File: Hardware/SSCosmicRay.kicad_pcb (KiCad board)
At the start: 2 copper layers, 80 x 50 mm, 142 parts, among them J1 ICSP-CORTEX, J2 CONN-9, U1 AD8616, U10 TPS73130, U2 AD8616, U3 AD8616, U4 STM32L151C6T6, U5 LM2903DT, U6 AD8616, U7 AD8616, U8 AOZ1280, U9 MAX5026, X1 8MHz

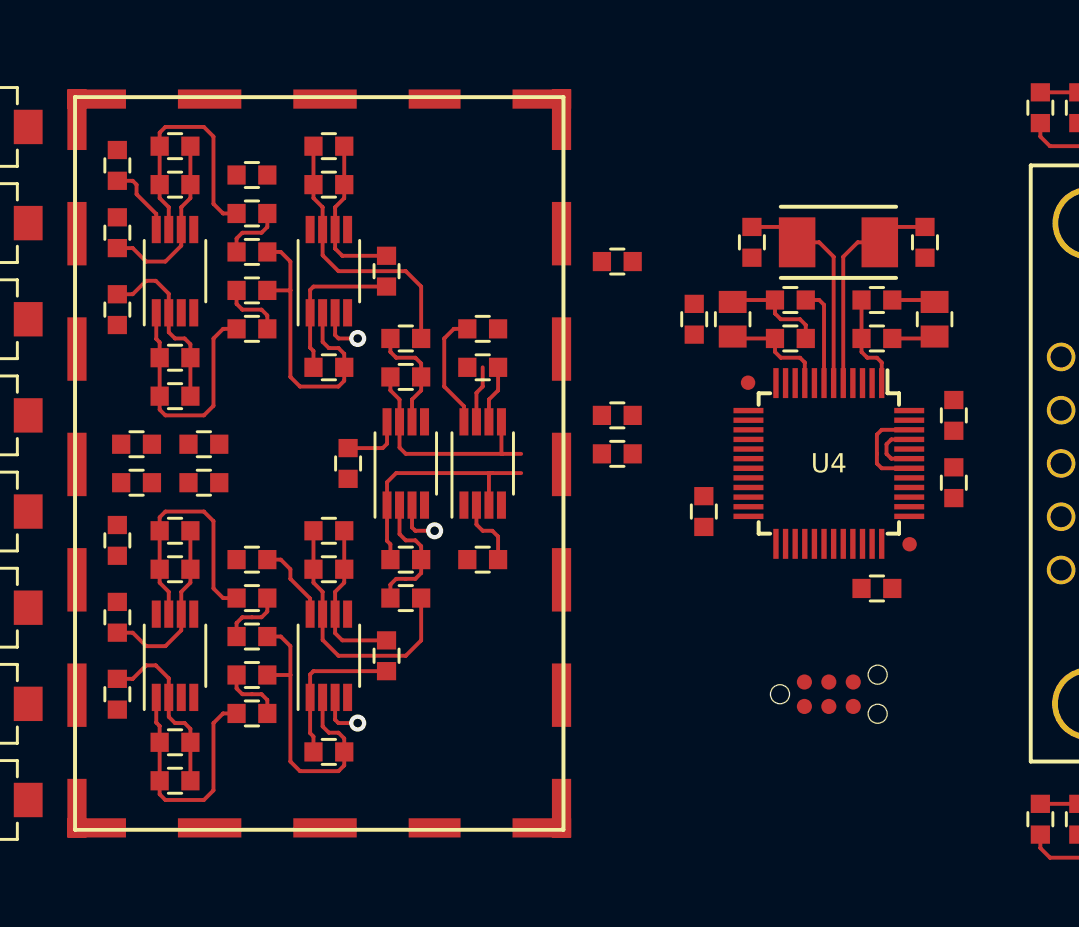
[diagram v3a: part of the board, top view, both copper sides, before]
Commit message: Equalize feedback network spacing
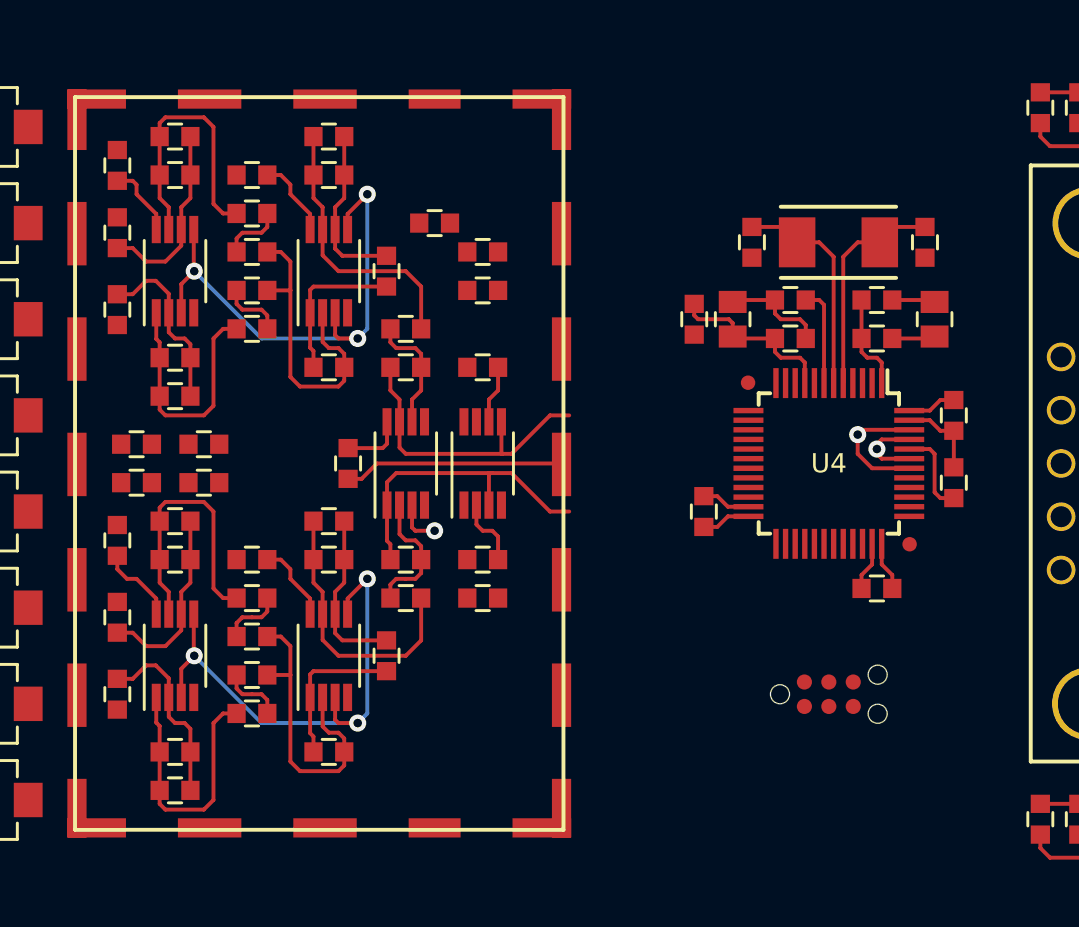
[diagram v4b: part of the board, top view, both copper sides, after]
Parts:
- moved R19 11.0 mm to (166.0, 67.0)
- moved R18 10.3 mm to (166.0, 85.0)
- moved R15 7.16 mm to (166.0, 69.0)
- moved C26 6.04 mm to (163.5, 65.5)
- moved C29 0.50 mm to (158.0, 83.0)
- moved C3 0.50 mm to (158.0, 63.0)
- moved C33 0.50 mm to (150.0, 93.0)
- moved C34 0.50 mm to (150.0, 83.0)
- moved C8 0.50 mm to (150.0, 63.0)
- moved R10 0.50 mm to (150.0, 61.0)
- moved R29 0.50 mm to (158.0, 81.0)
- moved R32 0.50 mm to (150.0, 95.0)
- moved R33 0.50 mm to (150.0, 81.0)
- moved R6 0.50 mm to (158.0, 61.0)
- moved R7 0.50 mm to (162.0, 71.0)
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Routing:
- net /Detector 1/Ref: track 7.22 -> 56.3 mm, vias 3 -> 7
- net GND: track 7.73 -> 28.7 mm
- net VAA: track 11.3 -> 19.6 mm
- net /Processor/BOOT: track 0.00 -> 4.55 mm
- net /Processor/A1: track 12.0 -> 15.8 mm
- net +3.3VADC: track 5.79 -> 9.25 mm
- net /Processor/A2: track 13.1 -> 16.4 mm
- net /Processor/DET1: track 2.97 -> 0.00 mm
- net /Processor/DO: track 5.07 -> 6.77 mm, vias 0 -> 1
- net +3.3V: track 12.4 -> 13.9 mm
- net N-000009: track 13.3 -> 14.3 mm
- net N-0000089: track 13.1 -> 14.1 mm
- net N-0000081: track 13.3 -> 14.3 mm
- net /Processor/DI: track 3.07 -> 4.07 mm, vias 0 -> 1
- net N-0000091: track 9.33 -> 9.83 mm
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
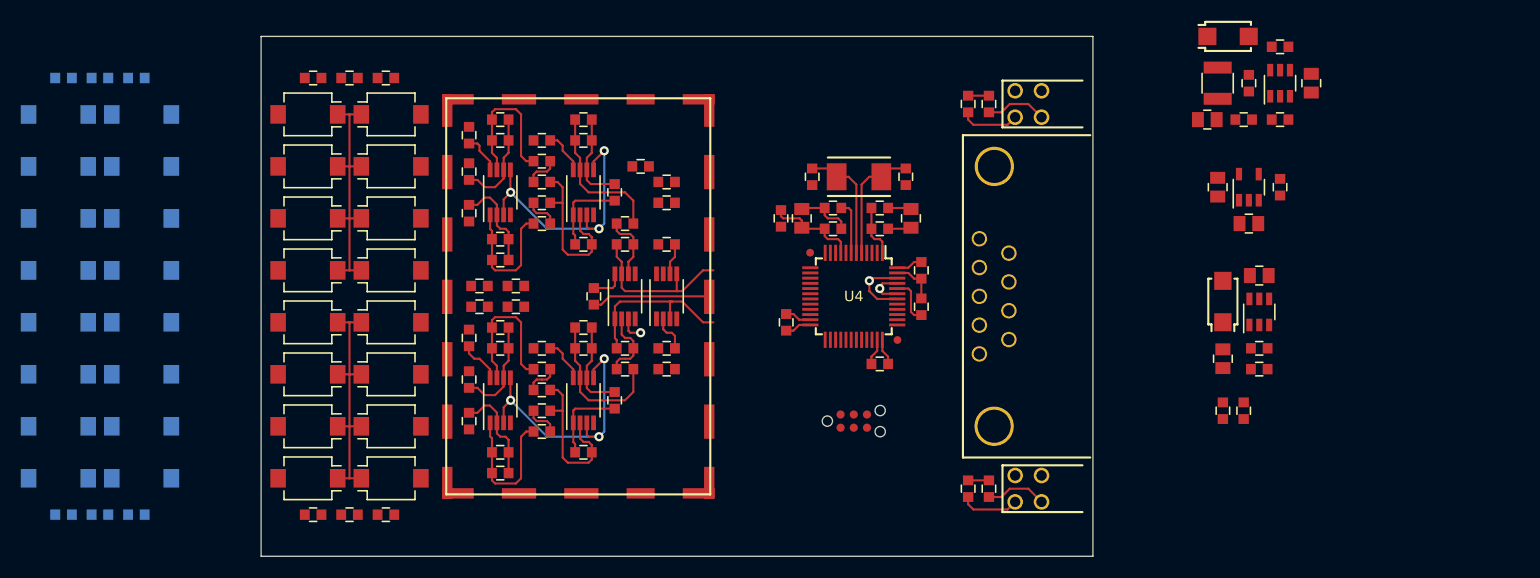
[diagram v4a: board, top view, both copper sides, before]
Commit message: Move interface connector to root sheet
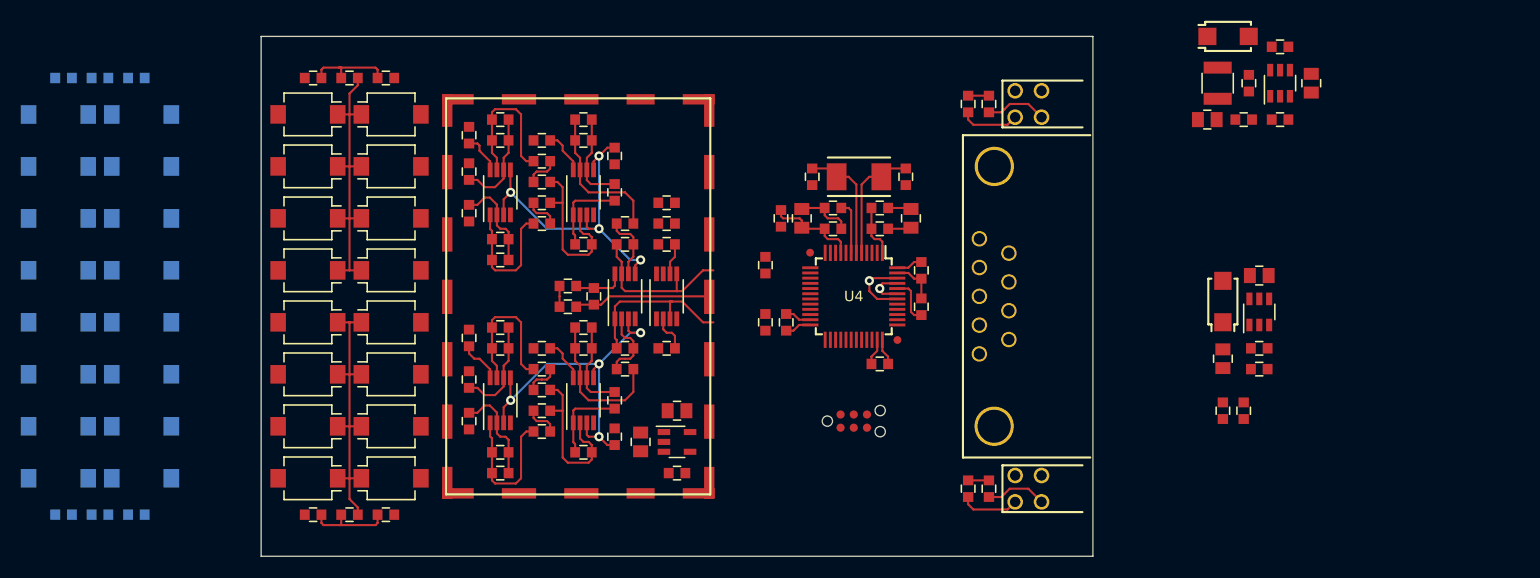
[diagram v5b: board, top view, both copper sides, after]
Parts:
- moved C45 64.2 mm to (167.0, 95.0), turned to 180 degrees
- moved C44 62.2 mm to (163.5, 92.0), turned to 270 degrees
- moved U10 60.2 mm to (167.0, 92.0), turned to 270 degrees
- moved C46 56.3 mm to (167.0, 89.0), turned to 180 degrees
- moved C47 19.5 mm to (161.0, 91.5), turned to 90 degrees
- moved R43 19.5 mm to (161.0, 64.5), turned to 90 degrees
- moved R19 12.4 mm to (175.5, 75.0), turned to 270 degrees
- moved R18 10.5 mm to (175.5, 80.5), turned to 90 degrees
- moved C30 5.00 mm to (156.5, 79.0)
- moved R42 5.00 mm to (156.5, 77.0)
- moved C26 4.30 mm to (166.0, 69.0)
- moved R15 2.00 mm to (166.0, 71.0)
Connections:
- net /Processor/AOUT renamed /Processor/AOut
- U4 pad 16: (no net) -> /Processor/DET1
- U4 pad 17: (no net) -> /Processor/A1
- U4 pad 19: (no net) -> /Processor/A2
- U4 pad 20: (no net) -> /Processor/DET2
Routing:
- net /Detector 1/Ref: track 56.3 -> 71.2 mm, vias 7 -> 8
- net N-0000029: track 0.00 -> 8.37 mm
- net N-0000025: track 0.00 -> 8.37 mm
- net /Detector 1/Det1B: track 24.1 -> 27.9 mm
- net /Detector 1/Det1A: track 24.1 -> 27.9 mm
- net VAA: track 19.6 -> 21.4 mm
- net GND: track 28.7 -> 30.5 mm

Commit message: Input voltage preregulation to extend input range
Closes #8
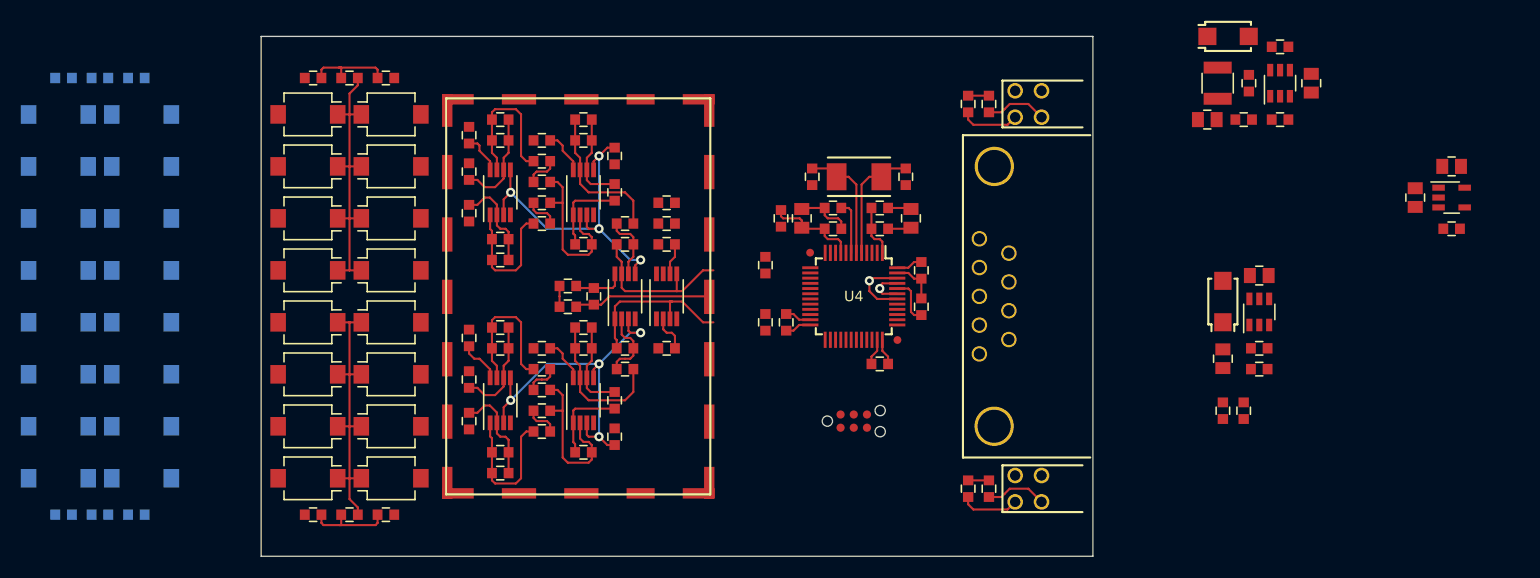
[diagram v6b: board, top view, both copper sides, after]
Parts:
- U10: value TPS73130 -> TPS73133
- moved C44 78.1 mm to (238.0, 68.5)
- moved C45 78.1 mm to (241.5, 71.5)
- moved C46 78.1 mm to (241.5, 65.5)
- moved U10 78.1 mm to (241.5, 68.5)
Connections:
- C12 pad 1: VAA -> +3.3V
- C35 pad 1: VAA -> +3.3V
- C38 pad 1: VAA -> +3.3V
- C4 pad 1: VAA -> +3.3V
- C40 pad 1: +BATT -> +5V
- C43 pad 1: +3.3V -> +5V
- C44 pad 1: +3.3V -> +5V
- C46 pad 1: VAA -> +3.3V
- C9 pad 1: VAA -> +3.3V
- L2 pad 2: +3.3V -> +5V
- R40 pad 2: +3.3V -> +5V
- R42 pad 2: VAA -> +3.3V
- U1 pad 8: VAA -> +3.3V
- U10 pad 1: +3.3V -> +5V
- U10 pad 3: +3.3V -> +5V
- U10 pad 5: VAA -> +3.3V
- U2 pad 8: VAA -> +3.3V
- U3 pad 8: VAA -> +3.3V
- U6 pad 8: VAA -> +3.3V
- U7 pad 8: VAA -> +3.3V
- U9 pad 4: +BATT -> +5V
- U9 pad 5: +BATT -> +5V
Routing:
- net VAA: track 21.4 -> 0.00 mm
- net +3.3V: track 13.9 -> 35.3 mm

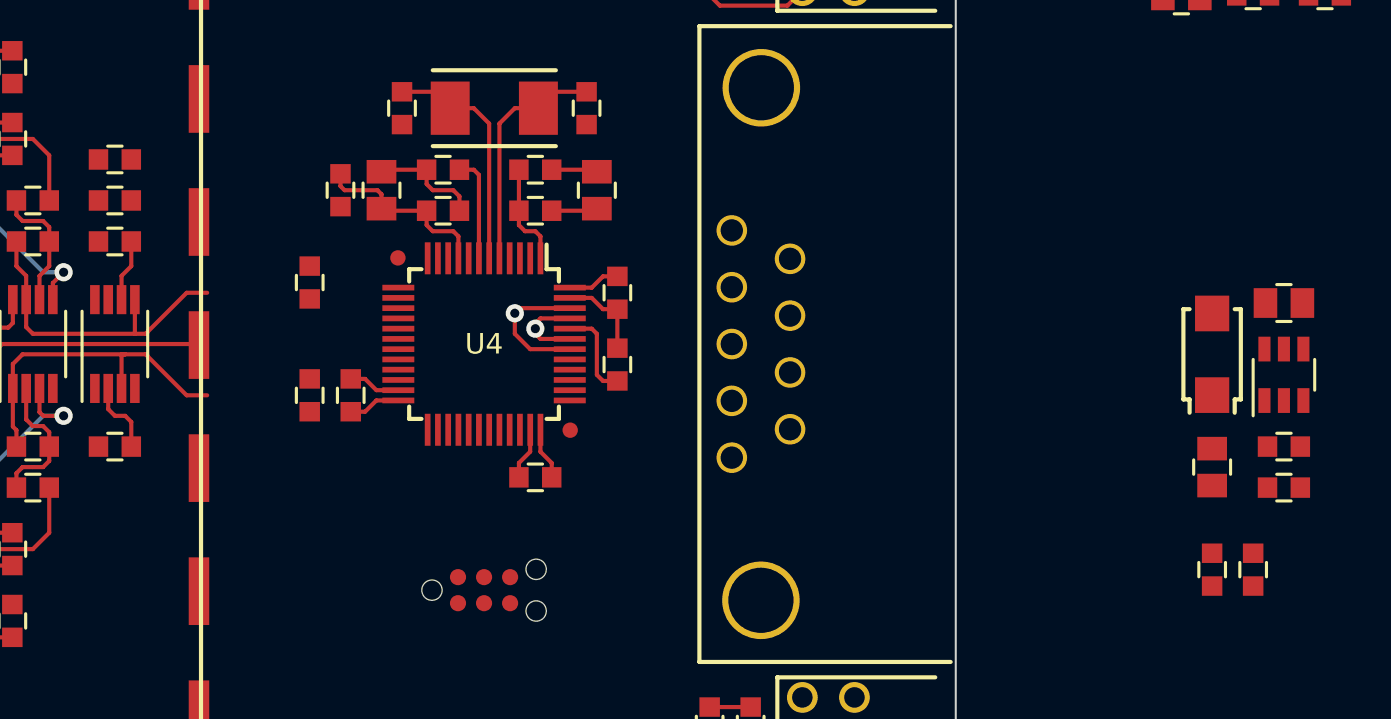
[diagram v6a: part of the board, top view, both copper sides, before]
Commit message: Connect interface pins
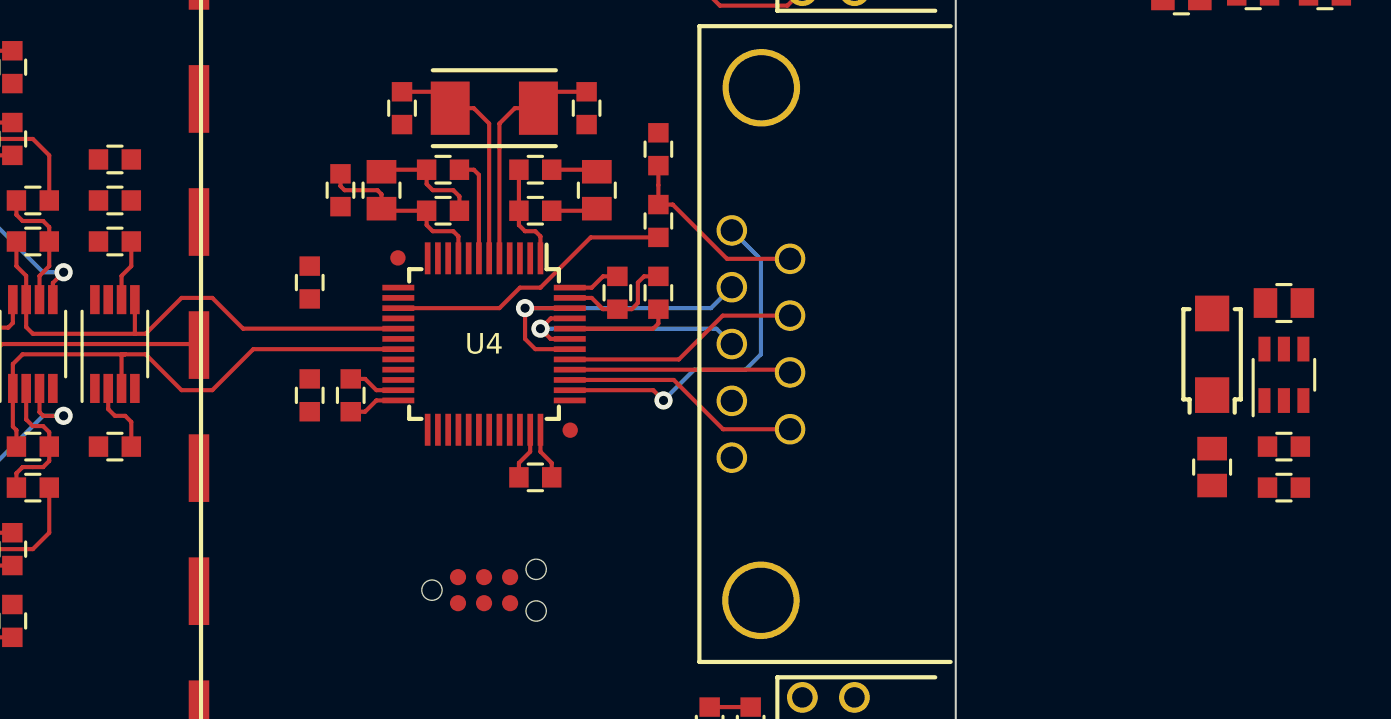
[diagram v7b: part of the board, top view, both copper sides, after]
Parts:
- moved C15 35.5 mm to (192.5, 68.5)
- moved R14 31.9 mm to (192.5, 72.0), turned to 270 degrees
- moved R16 4.03 mm to (192.5, 75.5)
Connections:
- J2 pad 1: (no net) -> /Processor/PS
- J2 pad 7: (no net) -> /Processor/CountC
- J2 pad 8: (no net) -> /Processor/Count1
- J2 pad 9: (no net) -> /Processor/Count2
- U4 pad 38: (no net) -> /Processor/PS
- U4 pad 39: (no net) -> /Processor/Count2
- U4 pad 40: (no net) -> /Processor/Count1
- U4 pad 41: (no net) -> /Processor/CountC
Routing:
- net /Processor/PS: track 0.00 -> 17.1 mm, vias 0 -> 1
- net /Processor/DAC: track 0.00 -> 14.1 mm
- net /Processor/Count2: track 0.00 -> 11.7 mm
- net /Processor/CountC: track 0.00 -> 11.6 mm
- net /Processor/Count1: track 0.00 -> 10.8 mm
- net /Processor/A2: track 16.4 -> 26.5 mm
- net /Processor/A1: track 15.8 -> 25.7 mm
- net /Processor/DO: track 6.77 -> 16.6 mm
- net /Processor/AOut: track 0.00 -> 9.42 mm
- net /Processor/DI: track 4.07 -> 12.9 mm
- net GND: track 30.5 -> 31.9 mm
- net /Processor/BOOT: track 4.55 -> 5.12 mm
